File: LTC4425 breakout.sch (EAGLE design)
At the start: 13 parts, among them IC1 LTC4425

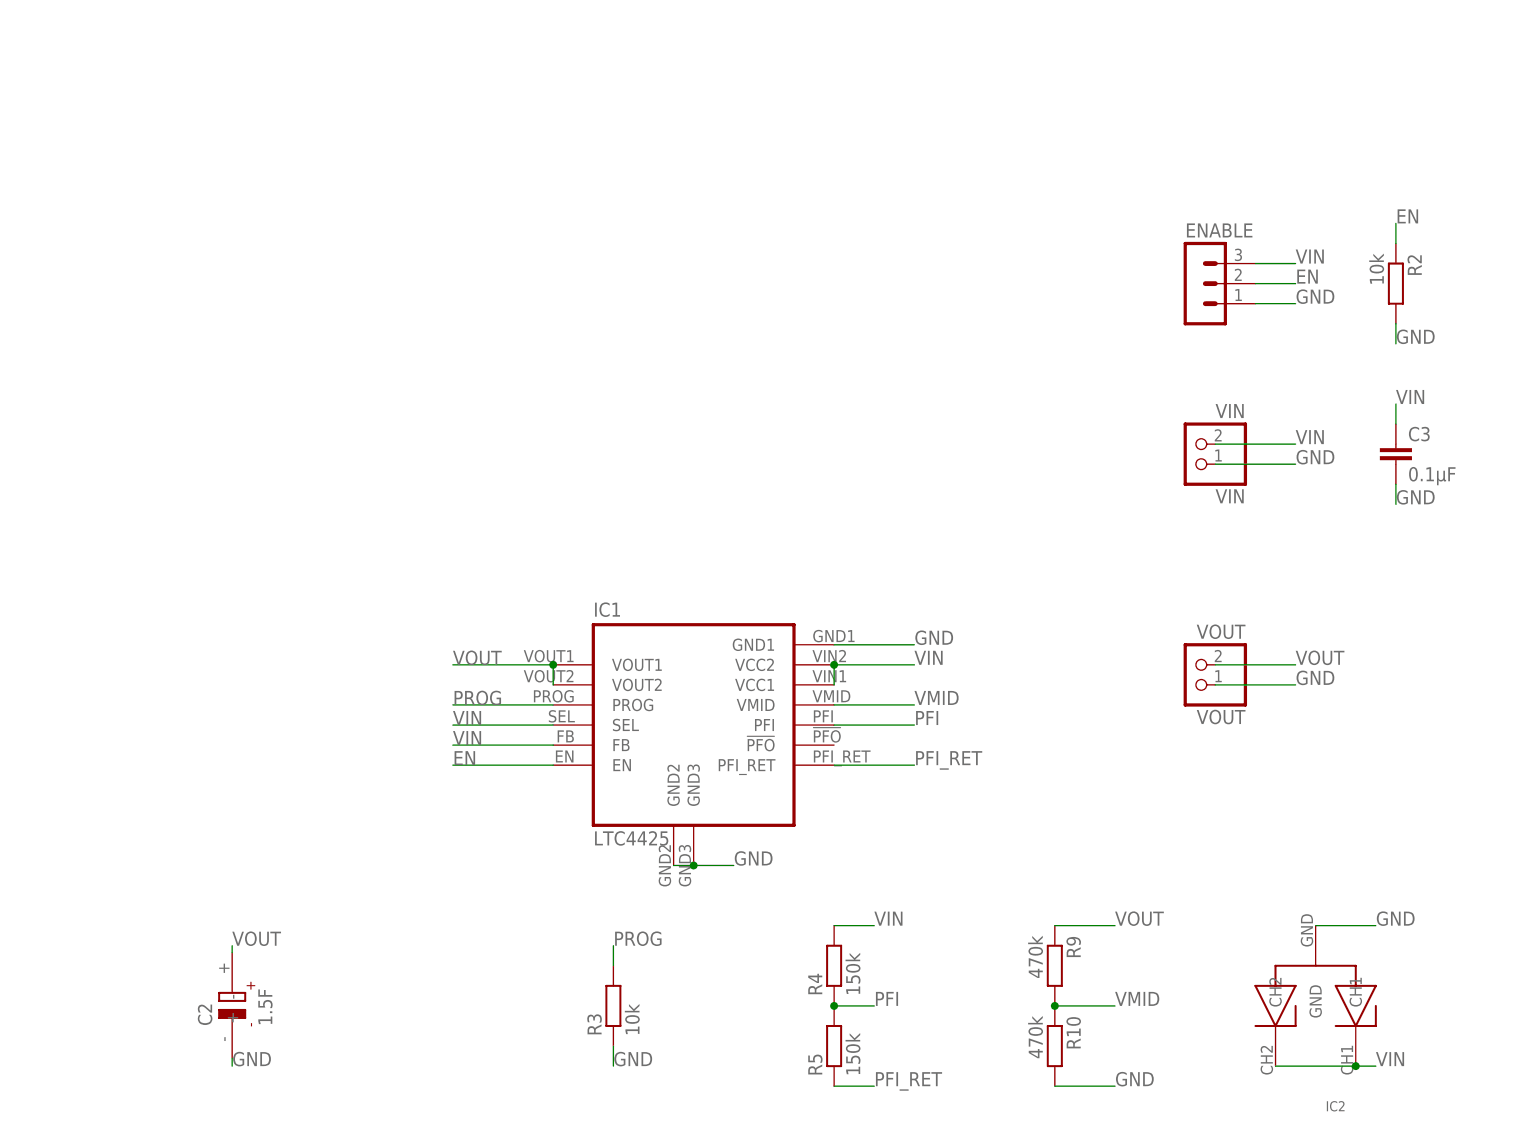
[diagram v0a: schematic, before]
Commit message: - updated LTC4425 breakout: replaced the supercap, modified tplace strings
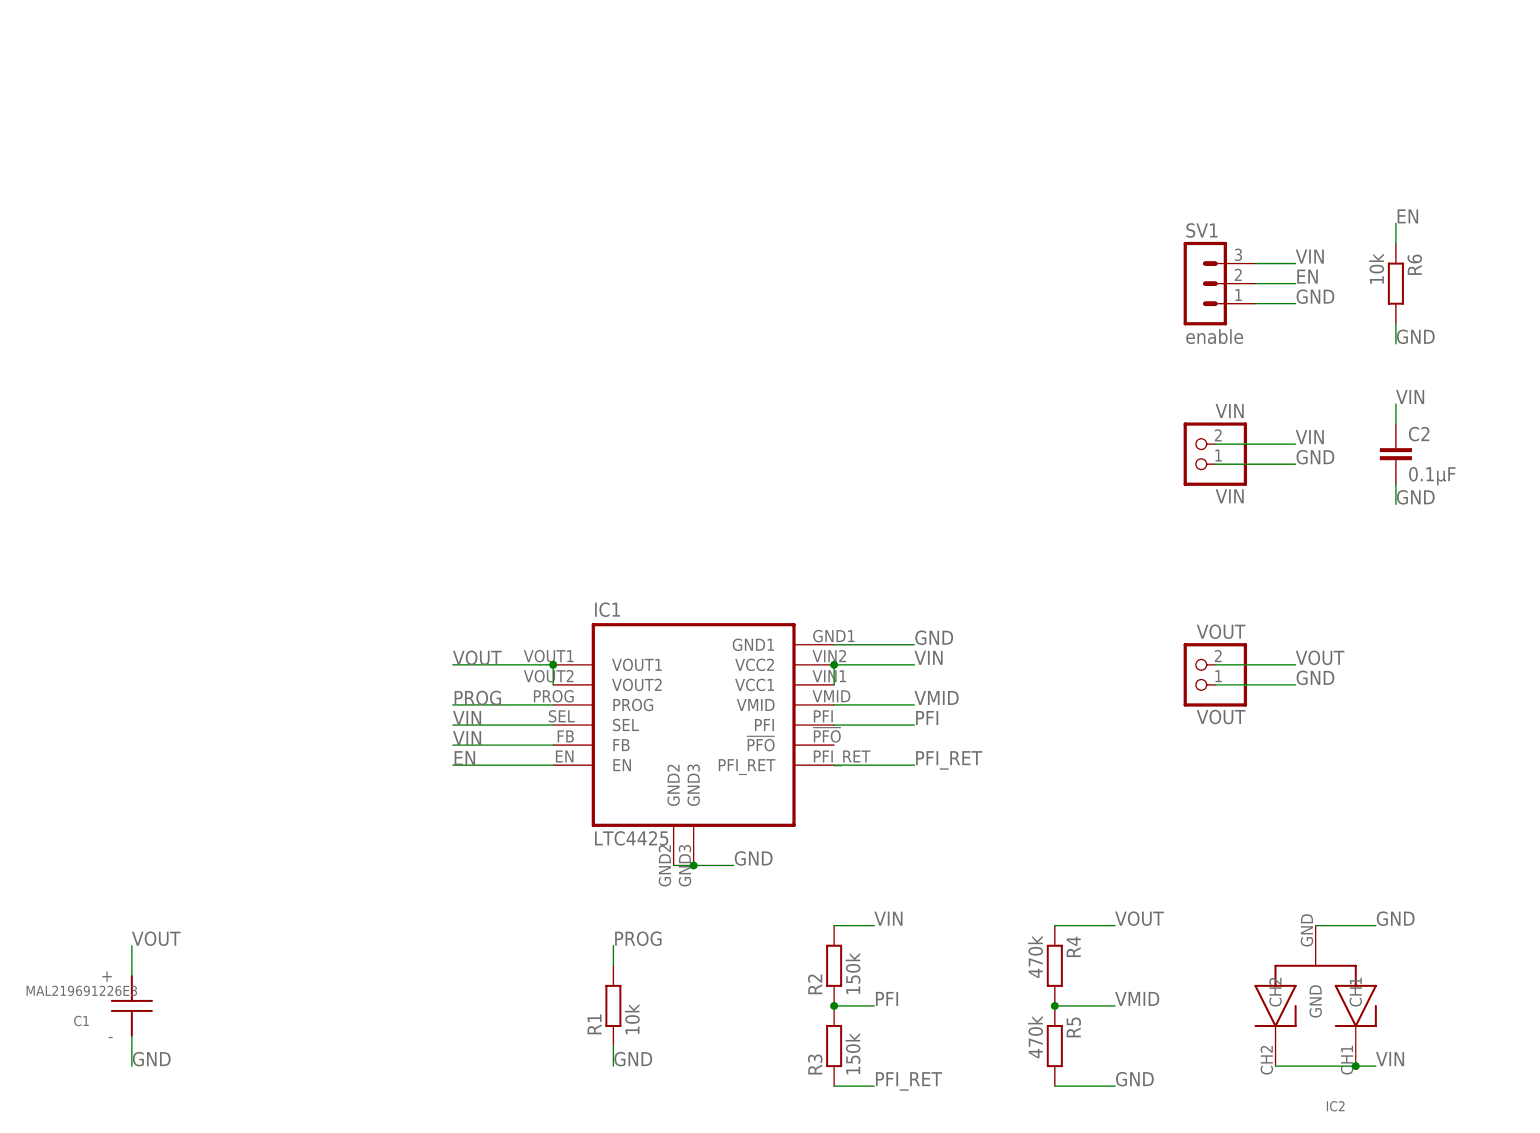
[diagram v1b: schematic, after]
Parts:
- removed C3: 0.1µF, rcl:C-EUC0805
- removed R10, R9: 470k, rcl:R-EU_R0805
- added C1: MAL219691226E3, MAL219691226E3 - Supercap:MAL219691226E3
- added R1, R6: 10k, rcl:R-EU_R0805
- C2: value 1.5F -> 0.1µF; device EECS5R5H155 Supercap:EECS5R5H155 -> rcl:C-EUC0805
- R2, R3: value 10k -> 150k
- R4, R5: value 150k -> 470k
- SV1: value (none) -> enable
- renumbered ENABLE to SV1
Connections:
- net EN: now also R6.1; no longer R2.1
- net GND: now also C1.-, C2.2, R1.1, R5.2, R6.2; no longer C2.-, C3.2, R10.2, R2.2, R3.1
- net PFI: now also R2.1, R3.2; no longer R4.1, R5.2
- net PFI_RET: now also R3.1; no longer R5.1
- net PROG: now also R1.2; no longer R3.2
- net VIN: now also C2.1, R2.2; no longer C3.1, R4.2
- net VMID: now also R4.2, R5.1; no longer R10.1, R9.2
- net VOUT: now also C1.+, R4.1; no longer C2.+, R9.1
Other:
- moved on the sheet: R2, R3, R4, R5
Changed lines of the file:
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@@
 <?xml version="1.0" encoding="utf-8"?>
 <!DOCTYPE eagle SYSTEM "eagle.dtd">
-<eagle version="8.5.0">
+<eagle version="8.6.1">
 <drawing>
 <settings>
@@
 <parts>
 <part name="IC1" library="LTC4425 Supercap Charger" deviceset="LTC4425" device=""/>
-<part name="R2" library="rcl" library_urn="urn:adsk.eagle:library:334" deviceset="R-EU_" device="R0805" package3d_urn="urn:adsk.eagle:package:23553/2" value="10k"/>
-<part name="R3" library="rcl" library_urn="urn:adsk.eagle:library:334" deviceset="R-EU_" device="R0805" package3d_urn="urn:adsk.eagle:package:23553/2" value="10k"/>
-<part name="C2" library="EECS5R5H155 Supercap" deviceset="EECS5R5H155" device="" value="1.5F"/>
-<part name="C3" library="rcl" library_urn="urn:adsk.eagle:library:334" deviceset="C-EU" device="C0805" package3d_urn="urn:adsk.eagle:package:23617/2" value="0.1µF"/>
-<part name="R4" library="rcl" library_urn="urn:adsk.eagle:library:334" deviceset="R-EU_" device="R0805" package3d_urn="urn:adsk.eagle:package:23553/2" value="150k"/>
-<part name="R5" library="rcl" library_urn="urn:adsk.eagle:library:334" deviceset="R-EU_" device="R0805" package3d_urn="urn:adsk.eagle:package:23553/2" value="150k"/>
-<part name="R9" library="rcl" library_urn="urn:adsk.eagle:library:334" deviceset="R-EU_" device="R0805" package3d_urn="urn:adsk.eagle:package:23553/2" value="470k"/>
-<part name="R10" library="rcl" library_urn="urn:adsk.eagle:library:334" deviceset="R-EU_" device="R0805" package3d_urn="urn:adsk.eagle:package:23553/2" value="470k"/>
+<part name="R6" library="rcl" library_urn="urn:adsk.eagle:library:334" deviceset="R-EU_" device="R0805" package3d_urn="urn:adsk.eagle:package:23553/2" value="10k"/>
+<part name="R1" library="rcl" library_urn="urn:adsk.eagle:library:334" deviceset="R-EU_" device="R0805" package3d_urn="urn:adsk.eagle:package:23553/2" value="10k"/>
+<part name="C2" library="rcl" library_urn="urn:adsk.eagle:library:334" deviceset="C-EU" device="C0805" package3d_urn="urn:adsk.eagle:package:23617/2" value="0.1µF"/>
+<part name="R2" library="rcl" library_urn="urn:adsk.eagle:library:334" deviceset="R-EU_" device="R0805" package3d_urn="urn:adsk.eagle:package:23553/2" value="150k"/>
+<part name="R3" library="rcl" library_urn="urn:adsk.eagle:library:334" deviceset="R-EU_" device="R0805" package3d_urn="urn:adsk.eagle:package:23553/2" value="150k"/>
+<part name="R4" library="rcl" library_urn="urn:adsk.eagle:library:334" deviceset="R-EU_" device="R0805" package3d_urn="urn:adsk.eagle:package:23553/2" value="470k"/>
+<part name="R5" library="rcl" library_urn="urn:adsk.eagle:library:334" deviceset="R-EU_" device="R0805" package3d_urn="urn:adsk.eagle:package:23553/2" value="470k"/>
 <part name="VIN" library="pinhead" library_urn="urn:adsk.eagle:library:325" deviceset="PINHD-1X2" device="" package3d_urn="urn:adsk.eagle:package:22435/2" value="VIN"/>
 <part name="VOUT" library="pinhead" library_urn="urn:adsk.eagle:library:325" deviceset="PINHD-1X2" device="" package3d_urn="urn:adsk.eagle:package:22435/2" value="VOUT"/>
 <part name="IC2" library="PESDxS2UT" deviceset="PESDXS2UT" device=""/>
-<part name="ENABLE" library="con-lstb" library_urn="urn:adsk.eagle:library:162" deviceset="MA03-1" device="" package3d_urn="urn:adsk.eagle:package:8339/1"/>
+<part name="SV1" library="con-lstb" library_urn="urn:adsk.eagle:library:162" deviceset="MA03-1" device="" package3d_urn="urn:adsk.eagle:package:8339/1" value="enable"/>
+<part name="C1" library="MAL219691226E3 - Supercap" deviceset="MAL219691226E3" device="" value="MAL219691226E3"/>
 </parts>
 <sheets>
@@
 <instances>
 <instance part="IC1" gate="G$1" x="40.64" y="33.02"/>
-<instance part="R2" gate="G$1" x="129.54" y="88.9" rot="R270"/>
-<instance part="R3" gate="G$1" x="30.48" y="-2.54" rot="R90"/>
-<instance part="C2" gate="G$1" x="-17.78" y="-2.54" rot="R90"/>
-<instance part="C3" gate="G$1" x="129.54" y="68.58" smashed="yes">
+<instance part="R6" gate="G$1" x="129.54" y="88.9" rot="R270"/>
+<instance part="R1" gate="G$1" x="30.48" y="-2.54" rot="R90"/>
+<instance part="C2" gate="G$1" x="129.54" y="68.58" smashed="yes">
 <attribute name="NAME" x="131.064" y="68.961" size="1.778" layer="95"/>
 <attribute name="VALUE" x="131.064" y="63.881" size="1.778" layer="96"/>
 </instance>
-<instance part="R4" gate="G$1" x="58.42" y="2.54" rot="R90"/>
-<instance part="R5" gate="G$1" x="58.42" y="-7.62" rot="R90"/>
-<instance part="R9" gate="G$1" x="86.36" y="2.54" rot="R270"/>
-<instance part="R10" gate="G$1" x="86.36" y="-7.62" rot="R270"/>
+<instance part="R2" gate="G$1" x="58.42" y="2.54" rot="R90"/>
+<instance part="R3" gate="G$1" x="58.42" y="-7.62" rot="R90"/>
+<instance part="R4" gate="G$1" x="86.36" y="2.54" rot="R270"/>
+<instance part="R5" gate="G$1" x="86.36" y="-7.62" rot="R270"/>
 <instance part="VIN" gate="G$1" x="104.14" y="68.58" rot="R180"/>
 <instance part="VOUT" gate="G$1" x="104.14" y="40.64" rot="R180"/>
 <instance part="IC2" gate="G$1" x="119.38" y="-7.62" rot="R180"/>
-<instance part="ENABLE" gate="G$1" x="104.14" y="88.9"/>
+<instance part="SV1" gate="G$1" x="104.14" y="88.9"/>
+<instance part="C1" gate="G$1" x="-30.48" y="-2.54" rot="R180"/>
 </instances>
 <busses>
@@
 </segment>
 <segment>
-<pinref part="R5" gate="G$1" pin="1"/>
+<pinref part="R3" gate="G$1" pin="1"/>
 <wire x1="58.42" y1="-12.7" x2="63.5" y2="-12.7" width="0.1524" layer="91"/>
 <label x="63.5" y="-12.7" size="1.778" layer="95"/>
@@
 </segment>
 <segment>
-<pinref part="R4" gate="G$1" pin="1"/>
-<pinref part="R5" gate="G$1" pin="2"/>
+<pinref part="R2" gate="G$1" pin="1"/>
+<pinref part="R3" gate="G$1" pin="2"/>
 <wire x1="58.42" y1="-2.54" x2="63.5" y2="-2.54" width="0.1524" layer="91"/>
 <junction x="58.42" y="-2.54"/>
@@
 </segment>
 <segment>
-<pinref part="R3" gate="G$1" pin="1"/>
+<pinref part="R1" gate="G$1" pin="1"/>
 <wire x1="30.48" y1="-7.62" x2="30.48" y2="-10.16" width="0.1524" layer="91"/>
 <label x="30.48" y="-10.16" size="1.778" layer="95"/>
 </segment>
 <segment>
-<pinref part="C3" gate="G$1" pin="2"/>
+<pinref part="C2" gate="G$1" pin="2"/>
 <wire x1="129.54" y1="63.5" x2="129.54" y2="60.96" width="0.1524" layer="91"/>
 <label x="129.54" y="60.96" size="1.778" layer="95"/>
 </segment>
 <segment>
-<pinref part="C2" gate="G$1" pin="-"/>
-<wire x1="-17.78" y1="-9.144" x2="-17.78" y2="-10.16" width="0.1524" layer="91"/>
-<label x="-17.78" y="-10.16" size="1.778" layer="95"/>
-</segment>
-<segment>
-<pinref part="R10" gate="G$1" pin="2"/>
+<pinref part="R5" gate="G$1" pin="2"/>
 <wire x1="86.36" y1="-12.7" x2="93.98" y2="-12.7" width="0.1524" layer="91"/>
 <label x="93.98" y="-12.7" size="1.778" layer="95"/>
@@
 </segment>
 <segment>
-<pinref part="R2" gate="G$1" pin="2"/>
+<pinref part="R6" gate="G$1" pin="2"/>
 <wire x1="129.54" y1="83.82" x2="129.54" y2="81.28" width="0.1524" layer="91"/>
 <label x="129.54" y="81.28" size="1.778" layer="95"/>
@@
 <wire x1="111.76" y1="86.36" x2="116.84" y2="86.36" width="0.1524" layer="91"/>
 <label x="116.84" y="86.36" size="1.778" layer="95"/>
-<pinref part="ENABLE" gate="G$1" pin="1"/>
+<pinref part="SV1" gate="G$1" pin="1"/>
+</segment>
+<segment>
+<wire x1="-30.48" y1="-10.16" x2="-30.48" y2="-6.35" width="0.1524" layer="91"/>
+<label x="-30.48" y="-10.16" size="1.778" layer="95"/>
+<pinref part="C1" gate="G$1" pin="-"/>
 </segment>
 </net>
@@
 </segment>
 <segment>
-<pinref part="C3" gate="G$1" pin="1"/>
+<pinref part="C2" gate="G$1" pin="1"/>
 <wire x1="129.54" y1="71.12" x2="129.54" y2="73.66" width="0.1524" layer="91"/>
 <label x="129.54" y="73.66" size="1.778" layer="95"/>
 </segment>
 <segment>
-<pinref part="R4" gate="G$1" pin="2"/>
+<pinref part="R2" gate="G$1" pin="2"/>
 <wire x1="58.42" y1="7.62" x2="63.5" y2="7.62" width="0.1524" layer="91"/>
 <label x="63.5" y="7.62" size="1.778" layer="95"/>
@@
 <wire x1="111.76" y1="91.44" x2="116.84" y2="91.44" width="0.1524" layer="91"/>
 <label x="116.84" y="91.44" size="1.778" layer="95"/>
-<pinref part="ENABLE" gate="G$1" pin="3"/>
+<pinref part="SV1" gate="G$1" pin="3"/>
 </segment>
 </net>
@@
 </segment>
 <segment>
-<pinref part="C2" gate="G$1" pin="+"/>
-<wire x1="-17.78" y1="4.191" x2="-17.78" y2="5.08" width="0.1524" layer="91"/>
-<label x="-17.78" y="5.08" size="1.778" layer="95"/>
-</segment>
-<segment>
-<pinref part="R9" gate="G$1" pin="1"/>
+<pinref part="R4" gate="G$1" pin="1"/>
 <wire x1="86.36" y1="7.62" x2="93.98" y2="7.62" width="0.1524" layer="91"/>
 <label x="93.98" y="7.62" size="1.778" layer="95"/>
@@
 <label x="116.84" y="40.64" size="1.778" layer="95"/>
 </segment>
+<segment>
+<wire x1="-30.48" y1="1.27" x2="-30.48" y2="5.08" width="0.1524" layer="91"/>
+<label x="-30.48" y="5.08" size="1.778" layer="95"/>
+<pinref part="C1" gate="G$1" pin="+"/>
+</segment>
 </net>
 <net name="VMID" class="0">
@@
 </segment>
 <segment>
-<pinref part="R9" gate="G$1" pin="2"/>
-<pinref part="R10" gate="G$1" pin="1"/>
+<pinref part="R4" gate="G$1" pin="2"/>
+<pinref part="R5" gate="G$1" pin="1"/>
 <wire x1="86.36" y1="-2.54" x2="93.98" y2="-2.54" width="0.1524" layer="91"/>
 <junction x="86.36" y="-2.54"/>
@@
 </segment>
 <segment>
-<pinref part="R3" gate="G$1" pin="2"/>
+<pinref part="R1" gate="G$1" pin="2"/>
 <wire x1="30.48" y1="2.54" x2="30.48" y2="5.08" width="0.1524" layer="91"/>
 <label x="30.48" y="5.08" size="1.778" layer="95"/>
@@
 </segment>
 <segment>
-<pinref part="R2" gate="G$1" pin="1"/>
+<pinref part="R6" gate="G$1" pin="1"/>
 <wire x1="129.54" y1="93.98" x2="129.54" y2="96.52" width="0.1524" layer="91"/>
 <label x="129.54" y="96.52" size="1.778" layer="95"/>
@@
 <wire x1="111.76" y1="88.9" x2="116.84" y2="88.9" width="0.1524" layer="91"/>
 <label x="116.84" y="88.9" size="1.778" layer="95"/>
-<pinref part="ENABLE" gate="G$1" pin="2"/>
-</segment>
-</net>
+<pinref part="SV1" gate="G$1" pin="2"/>
+</segment>
+</net>

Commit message: - removed supercap from board and made it generic - updated gerbers and design block
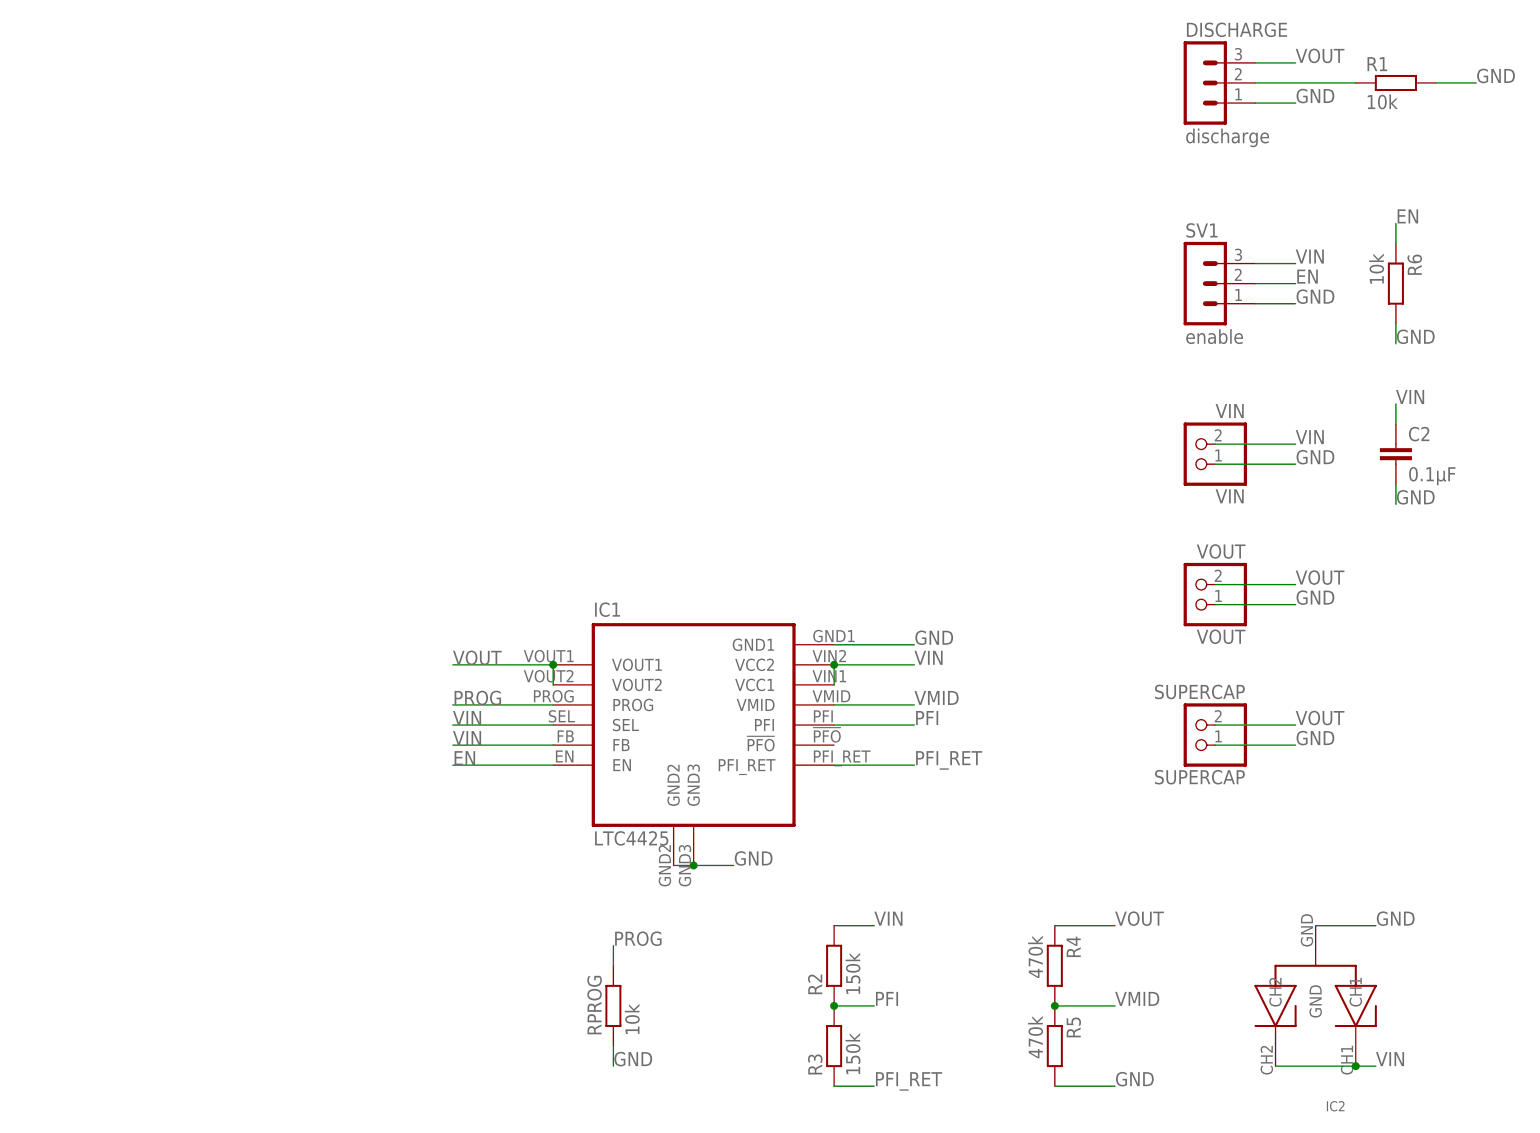
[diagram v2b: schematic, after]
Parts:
- removed C1: MAL219691226E3, MAL219691226E3 - Supercap:MAL219691226E3
- added DISCHARGE: discharge, con-lstb:MA03-1
- added RPROG: 10k, rcl:R-EU_R0805
- added SUPERCAP: SUPERCAP, pinhead:PINHD-1X2
- R1: device rcl:R-EU_R0805 -> rcl:R-EU_R1206
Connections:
- new net N$2: DISCHARGE.2, R1.1
- net GND: now also DISCHARGE.1, R1.2, RPROG.1, SUPERCAP.1; no longer C1.-, R1.1
- net PROG: now also RPROG.2; no longer R1.2
- net VOUT: now also DISCHARGE.3, SUPERCAP.2; no longer C1.+
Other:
- moved on the sheet: R1, VOUT
